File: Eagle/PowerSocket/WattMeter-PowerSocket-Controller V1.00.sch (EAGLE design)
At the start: 44 parts, among them IC1 ADE7953ACPZLONGPADS, Q1 535-10200-1-ND

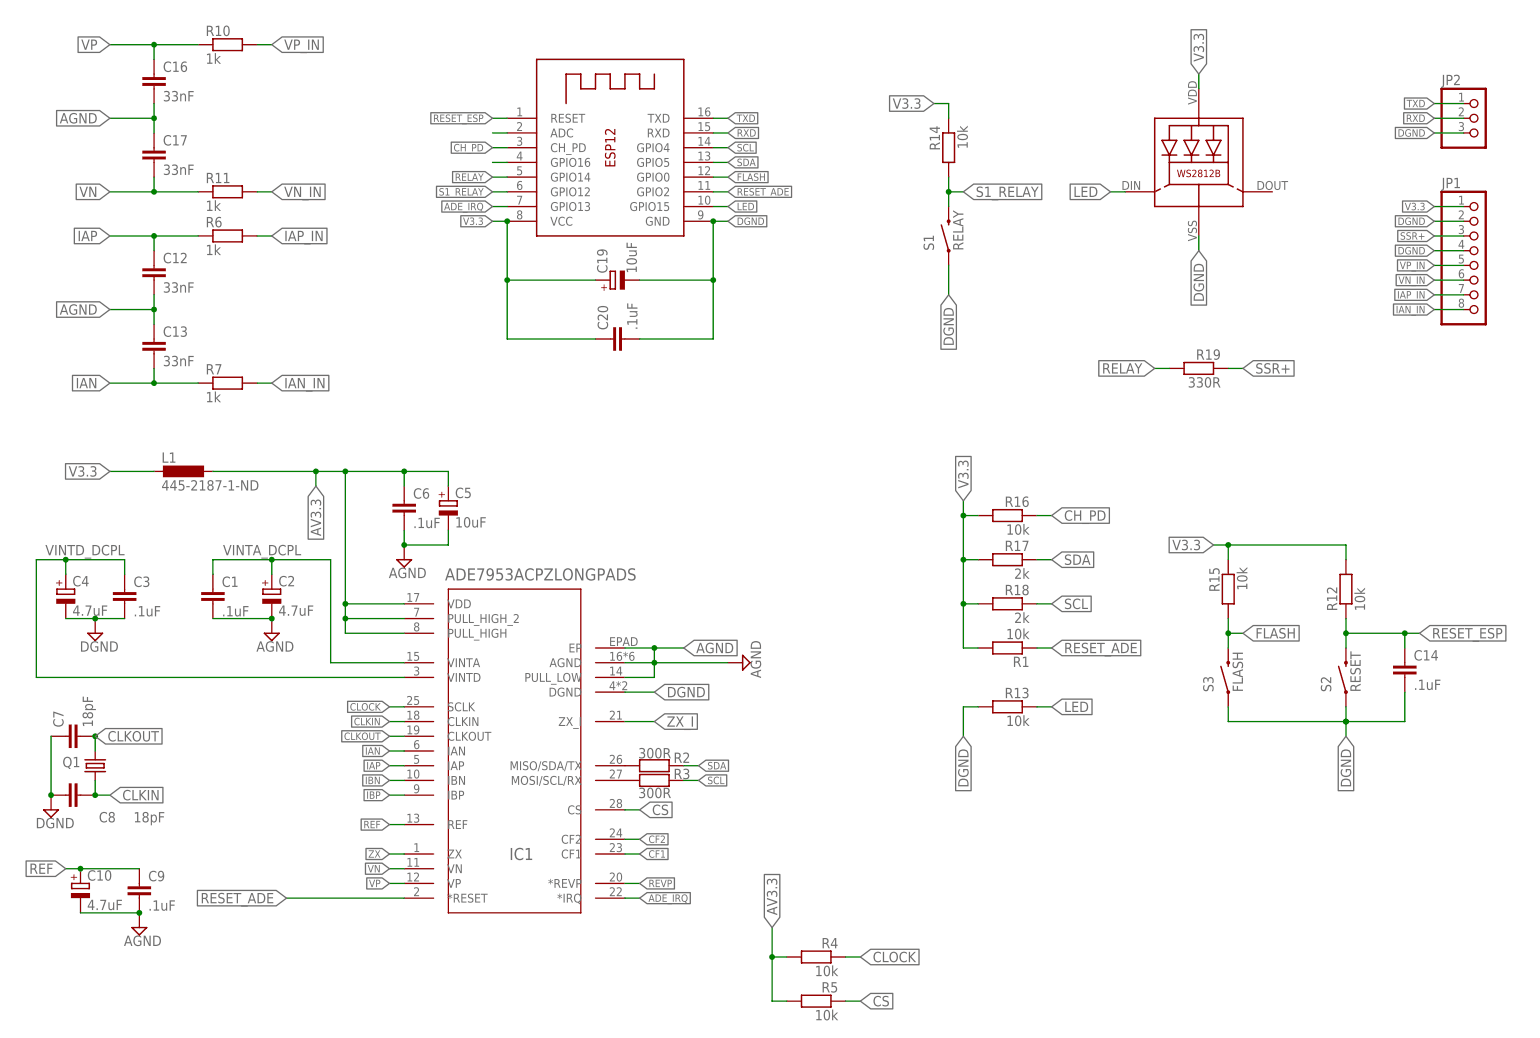
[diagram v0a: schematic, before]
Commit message: Update Eagle PowerSocket
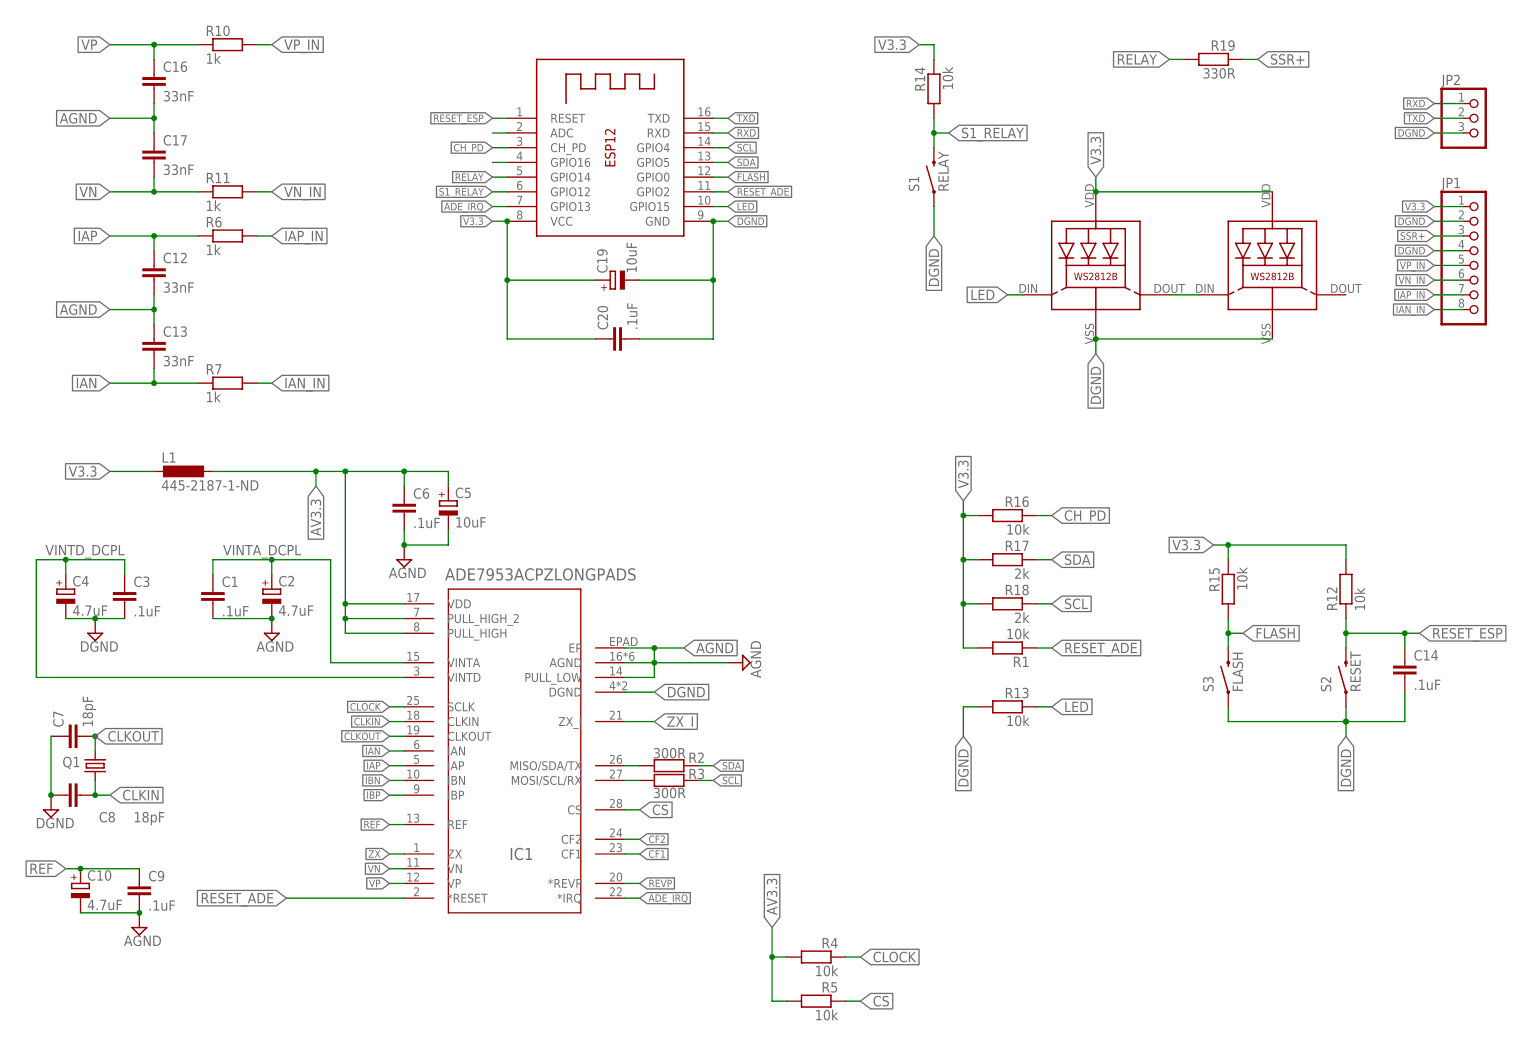
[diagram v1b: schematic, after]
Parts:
- added LED2: WS2812B, WS2812B:WS2812B
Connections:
- net PIN26_MISO_SDA_TX renamed SDA_
- net PIN27_MOSI_SCL_RX renamed SCL_
- new net N$4: LED1.DO, LED2.DI
- net DGND: now also LED2.GND
- net RXD: now also JP2.1; no longer JP2.2
- net TXD: now also JP2.2; no longer JP2.1
- net V3.3: now also LED2.VDD
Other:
- moved on the sheet: R14, R19, R2, R3, S1
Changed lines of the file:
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@@
 <?xml version="1.0" encoding="utf-8"?>
 <!DOCTYPE eagle SYSTEM "eagle.dtd">
-<eagle version="7.7.0">
+<eagle version="8.0.0">
 <drawing>
 <settings>
@@
 <part name="R19" library="resistor" deviceset="R-US_" device="R0805" value="330R"/>
 <part name="C14" library="resistor" deviceset="C-EU" device="C0805K" value=".1uF"/>
+<part name="LED2" library="WS2812B" deviceset="WS2812B" device=""/>
 </parts>
 <sheets>
@@
 </instance>
 <instance part="SUPPLY11" gate="G$1" x="10.16" y="40.64"/>
-<instance part="R2" gate="G$1" x="114.3" y="48.26" smashed="yes">
-<attribute name="NAME" x="117.602" y="48.7426" size="1.778" layer="95"/>
-<attribute name="VALUE" x="111.506" y="49.53" size="1.778" layer="96"/>
+<instance part="R2" gate="G$1" x="116.84" y="48.26" smashed="yes">
+<attribute name="NAME" x="120.142" y="48.7426" size="1.778" layer="95"/>
+<attribute name="VALUE" x="114.046" y="49.53" size="1.778" layer="96"/>
 </instance>
-<instance part="R3" gate="G$1" x="114.3" y="45.72" smashed="yes">
-<attribute name="NAME" x="117.602" y="45.9486" size="1.778" layer="95"/>
-<attribute name="VALUE" x="111.506" y="42.672" size="1.778" layer="96"/>
+<instance part="R3" gate="G$1" x="116.84" y="45.72" smashed="yes">
+<attribute name="NAME" x="120.142" y="45.9486" size="1.778" layer="95"/>
+<attribute name="VALUE" x="114.046" y="42.672" size="1.778" layer="96"/>
 </instance>
 <instance part="C2" gate="G$1" x="48.26" y="78.74"/>
@@
 <instance part="S2" gate="G$1" x="233.68" y="63.5" rot="R90"/>
 <instance part="S3" gate="G$1" x="213.36" y="63.5" rot="R90"/>
-<instance part="S1" gate="G$1" x="165.1" y="139.7" rot="R90"/>
-<instance part="LED1" gate="G$1" x="208.28" y="149.86"/>
+<instance part="S1" gate="G$1" x="162.56" y="149.86" rot="R90"/>
+<instance part="LED1" gate="G$1" x="190.5" y="132.08"/>
 <instance part="R12" gate="G$1" x="233.68" y="78.74" rot="R90"/>
 <instance part="R15" gate="G$1" x="213.36" y="78.74" rot="MR270"/>
@@
 <instance part="R18" gate="G$1" x="175.26" y="76.2" rot="MR0"/>
 <instance part="R13" gate="G$1" x="175.26" y="58.42" rot="MR0"/>
-<instance part="R14" gate="G$1" x="165.1" y="154.94" rot="MR270"/>
+<instance part="R14" gate="G$1" x="162.56" y="165.1" rot="MR270"/>
 <instance part="C19" gate="G$1" x="106.68" y="132.08" rot="R90"/>
 <instance part="C20" gate="G$1" x="106.68" y="121.92" rot="R90"/>
 <instance part="JP2" gate="A" x="256.54" y="160.02"/>
 <instance part="JP1" gate="A" x="256.54" y="134.62"/>
-<instance part="R19" gate="G$1" x="208.28" y="116.84" rot="MR0"/>
+<instance part="R19" gate="G$1" x="210.82" y="170.18" rot="MR0"/>
 <instance part="C14" gate="G$1" x="243.84" y="66.04"/>
+<instance part="LED2" gate="G$1" x="220.98" y="132.08"/>
 </instances>
 <busses>
@@
 </segment>
 <segment>
-<label x="165.1" y="129.54" size="1.778" layer="95" rot="R270" xref="yes"/>
+<label x="162.56" y="139.7" size="1.778" layer="95" rot="R270" xref="yes"/>
 <pinref part="S1" gate="G$1" pin="1"/>
-<wire x1="165.1" y1="129.54" x2="165.1" y2="134.62" width="0.1524" layer="91"/>
+<wire x1="162.56" y1="139.7" x2="162.56" y2="144.78" width="0.1524" layer="91"/>
 </segment>
 <segment>
@@
 <segment>
 <pinref part="LED1" gate="G$1" pin="GND"/>
-<wire x1="208.28" y1="139.7" x2="208.28" y2="137.16" width="0.1524" layer="91"/>
-<label x="208.28" y="137.16" size="1.778" layer="95" rot="R270" xref="yes"/>
+<wire x1="190.5" y1="121.92" x2="190.5" y2="119.38" width="0.1524" layer="91"/>
+<label x="190.5" y="119.38" size="1.778" layer="95" rot="R270" xref="yes"/>
+<pinref part="LED2" gate="G$1" pin="GND"/>
+<wire x1="190.5" y1="121.92" x2="220.98" y2="121.92" width="0.1524" layer="91"/>
+<junction x="190.5" y="121.92"/>
 </segment>
 </net>
@@
 </segment>
 <segment>
-<wire x1="165.1" y1="162.56" x2="165.1" y2="160.02" width="0.1524" layer="91"/>
-<wire x1="165.1" y1="162.56" x2="162.56" y2="162.56" width="0.1524" layer="91"/>
-<label x="162.56" y="162.56" size="1.778" layer="95" rot="R180" xref="yes"/>
+<wire x1="162.56" y1="172.72" x2="162.56" y2="170.18" width="0.1524" layer="91"/>
+<wire x1="162.56" y1="172.72" x2="160.02" y2="172.72" width="0.1524" layer="91"/>
+<label x="160.02" y="172.72" size="1.778" layer="95" rot="R180" xref="yes"/>
 <pinref part="R14" gate="G$1" pin="1"/>
 </segment>
@@
 <segment>
 <pinref part="LED1" gate="G$1" pin="VDD"/>
-<wire x1="208.28" y1="165.1" x2="208.28" y2="167.64" width="0.1524" layer="91"/>
-<label x="208.28" y="167.64" size="1.778" layer="95" rot="R90" xref="yes"/>
+<wire x1="190.5" y1="147.32" x2="190.5" y2="149.86" width="0.1524" layer="91"/>
+<label x="190.5" y="149.86" size="1.778" layer="95" rot="R90" xref="yes"/>
+<pinref part="LED2" gate="G$1" pin="VDD"/>
+<wire x1="190.5" y1="147.32" x2="220.98" y2="147.32" width="0.1524" layer="91"/>
+<junction x="190.5" y="147.32"/>
 </segment>
 </net>
@@
 <segment>
 <pinref part="R2" gate="G$1" pin="2"/>
-<wire x1="119.38" y1="48.26" x2="121.92" y2="48.26" width="0.1524" layer="91"/>
-<label x="121.92" y="48.26" size="1.27" layer="95" xref="yes"/>
+<wire x1="121.92" y1="48.26" x2="124.46" y2="48.26" width="0.1524" layer="91"/>
+<label x="124.46" y="48.26" size="1.27" layer="95" xref="yes"/>
 </segment>
 <segment>
@@
 <segment>
 <pinref part="R3" gate="G$1" pin="2"/>
-<wire x1="119.38" y1="45.72" x2="121.92" y2="45.72" width="0.1524" layer="91"/>
-<label x="121.92" y="45.72" size="1.27" layer="95" xref="yes"/>
+<wire x1="121.92" y1="45.72" x2="124.46" y2="45.72" width="0.1524" layer="91"/>
+<label x="124.46" y="45.72" size="1.27" layer="95" xref="yes"/>
 </segment>
 <segment>
@@
 </segment>
 </net>
-<net name="PIN26_MISO_SDA_TX" class="2">
+<net name="SDA_" class="2">
 <segment>
 <pinref part="R2" gate="G$1" pin="1"/>
 <pinref part="IC1" gate="A" pin="MISO/SDA/TX"/>
-</segment>
-</net>
-<net name="PIN27_MOSI_SCL_RX" class="2">
+<wire x1="111.76" y1="48.26" x2="109.22" y2="48.26" width="0.1524" layer="91"/>
+</segment>
+</net>
+<net name="SCL_" class="2">
 <segment>
 <pinref part="R3" gate="G$1" pin="1"/>
 <pinref part="IC1" gate="A" pin="MOSI/SCL/RX"/>
+<wire x1="111.76" y1="45.72" x2="109.22" y2="45.72" width="0.1524" layer="91"/>
 </segment>
 </net>
@@
 </segment>
 <segment>
+<pinref part="JP2" gate="A" pin="2"/>
+<wire x1="254" y1="160.02" x2="248.92" y2="160.02" width="0.1524" layer="91"/>
+<label x="248.92" y="160.02" size="1.27" layer="95" rot="R180" xref="yes"/>
+</segment>
+</net>
+<net name="RXD" class="0">
+<segment>
+<pinref part="X1" gate="G$1" pin="RXD"/>
+<wire x1="124.46" y1="157.48" x2="127" y2="157.48" width="0.1524" layer="91"/>
+<label x="127" y="157.48" size="1.27" layer="95" xref="yes"/>
+</segment>
+<segment>
 <pinref part="JP2" gate="A" pin="1"/>
 <wire x1="254" y1="162.56" x2="248.92" y2="162.56" width="0.1524" layer="91"/>
@@
 </segment>
 </net>
-<net name="RXD" class="0">
-<segment>
-<pinref part="X1" gate="G$1" pin="RXD"/>
-<wire x1="124.46" y1="157.48" x2="127" y2="157.48" width="0.1524" layer="91"/>
-<label x="127" y="157.48" size="1.27" layer="95" xref="yes"/>
-</segment>
-<segment>
-<pinref part="JP2" gate="A" pin="2"/>
-<wire x1="254" y1="160.02" x2="248.92" y2="160.02" width="0.1524" layer="91"/>
-<label x="248.92" y="160.02" size="1.27" layer="95" rot="R180" xref="yes"/>
-</segment>
-</net>
 <net name="LED" class="0">
 <segment>
@@
 <segment>
 <pinref part="LED1" gate="G$1" pin="DI"/>
-<wire x1="195.58" y1="147.32" x2="193.04" y2="147.32" width="0.1524" layer="91"/>
-<label x="193.04" y="147.32" size="1.778" layer="95" rot="R180" xref="yes"/>
+<wire x1="177.8" y1="129.54" x2="175.26" y2="129.54" width="0.1524" layer="91"/>
+<label x="175.26" y="129.54" size="1.778" layer="95" rot="R180" xref="yes"/>
 </segment>
 <segment>
@@
 <segment>
 <pinref part="R19" gate="G$1" pin="2"/>
-<wire x1="203.2" y1="116.84" x2="200.66" y2="116.84" width="0.1524" layer="91"/>
-<label x="200.66" y="116.84" size="1.778" layer="95" rot="R180" xref="yes"/>
+<wire x1="205.74" y1="170.18" x2="203.2" y2="170.18" width="0.1524" layer="91"/>
+<label x="203.2" y="170.18" size="1.778" layer="95" rot="R180" xref="yes"/>
 </segment>
 </net>
@@
 <pinref part="R14" gate="G$1" pin="2"/>
 <pinref part="S1" gate="G$1" pin="2"/>
-<wire x1="165.1" y1="149.86" x2="165.1" y2="147.32" width="0.1524" layer="91"/>
-<wire x1="165.1" y1="147.32" x2="165.1" y2="144.78" width="0.1524" layer="91"/>
-<wire x1="165.1" y1="147.32" x2="167.64" y2="147.32" width="0.1524" layer="91"/>
-<junction x="165.1" y="147.32"/>
-<label x="167.64" y="147.32" size="1.778" layer="95" xref="yes"/>
+<wire x1="162.56" y1="160.02" x2="162.56" y2="157.48" width="0.1524" layer="91"/>
+<wire x1="162.56" y1="157.48" x2="162.56" y2="154.94" width="0.1524" layer="91"/>
+<wire x1="162.56" y1="157.48" x2="165.1" y2="157.48" width="0.1524" layer="91"/>
+<junction x="162.56" y="157.48"/>
+<label x="165.1" y="157.48" size="1.778" layer="95" xref="yes"/>
 </segment>
 <segment>
@@
 <segment>
 <pinref part="R19" gate="G$1" pin="1"/>
-<wire x1="213.36" y1="116.84" x2="215.9" y2="116.84" width="0.1524" layer="91"/>
-<label x="215.9" y="116.84" size="1.778" layer="95" xref="yes"/>
-</segment>
-</net>
+<wire x1="215.9" y1="170.18" x2="218.44" y2="170.18" width="0.1524" layer="91"/>
+<label x="218.44" y="170.18" size="1.778" layer="95" xref="yes"/>
+</segment>
+</net>
+<net name="N$4" class="0">
+<segment>
+<pinref part="LED1" gate="G$1" pin="DO"/>
+<pinref part="LED2" gate="G$1" pin="DI"/>
+<wire x1="203.2" y1="129.54" x2="208.28" y2="129.54" width="0.1524" layer="91"/>
+</segment>
+</net>
